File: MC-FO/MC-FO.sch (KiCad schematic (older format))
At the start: 1 part, among them J1 DB25_Female

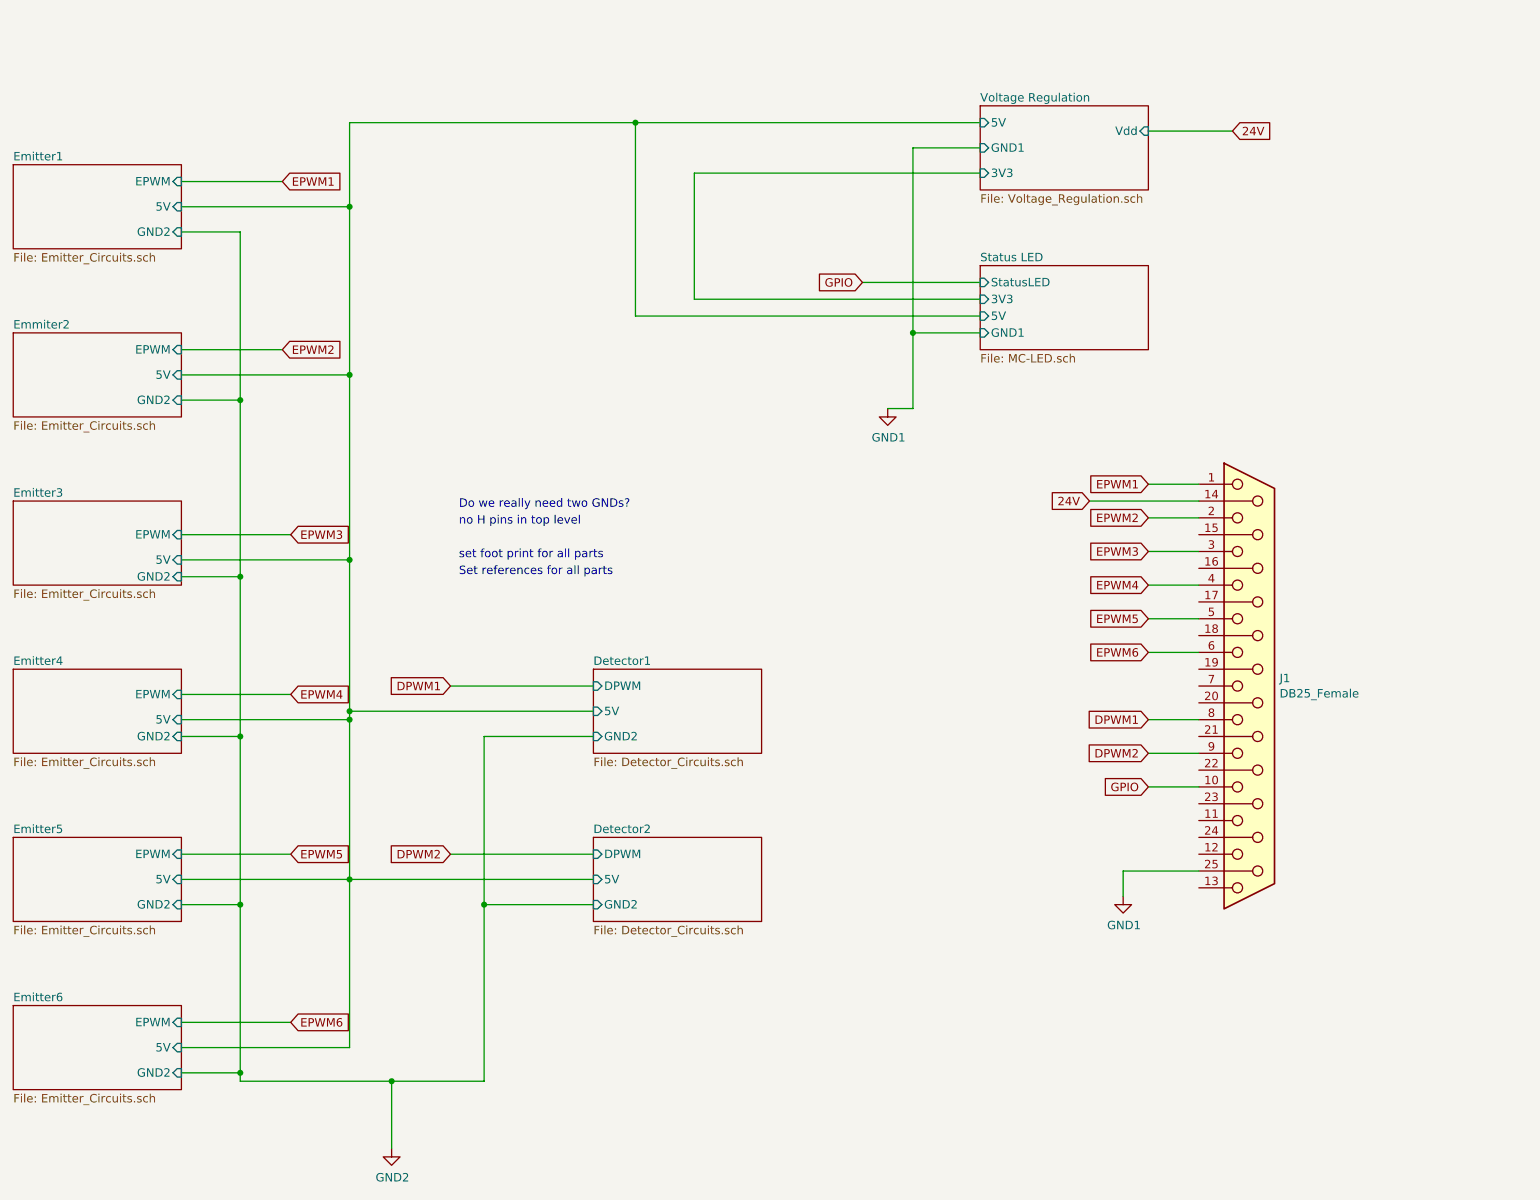
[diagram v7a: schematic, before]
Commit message: floating pins fix, signal name updates
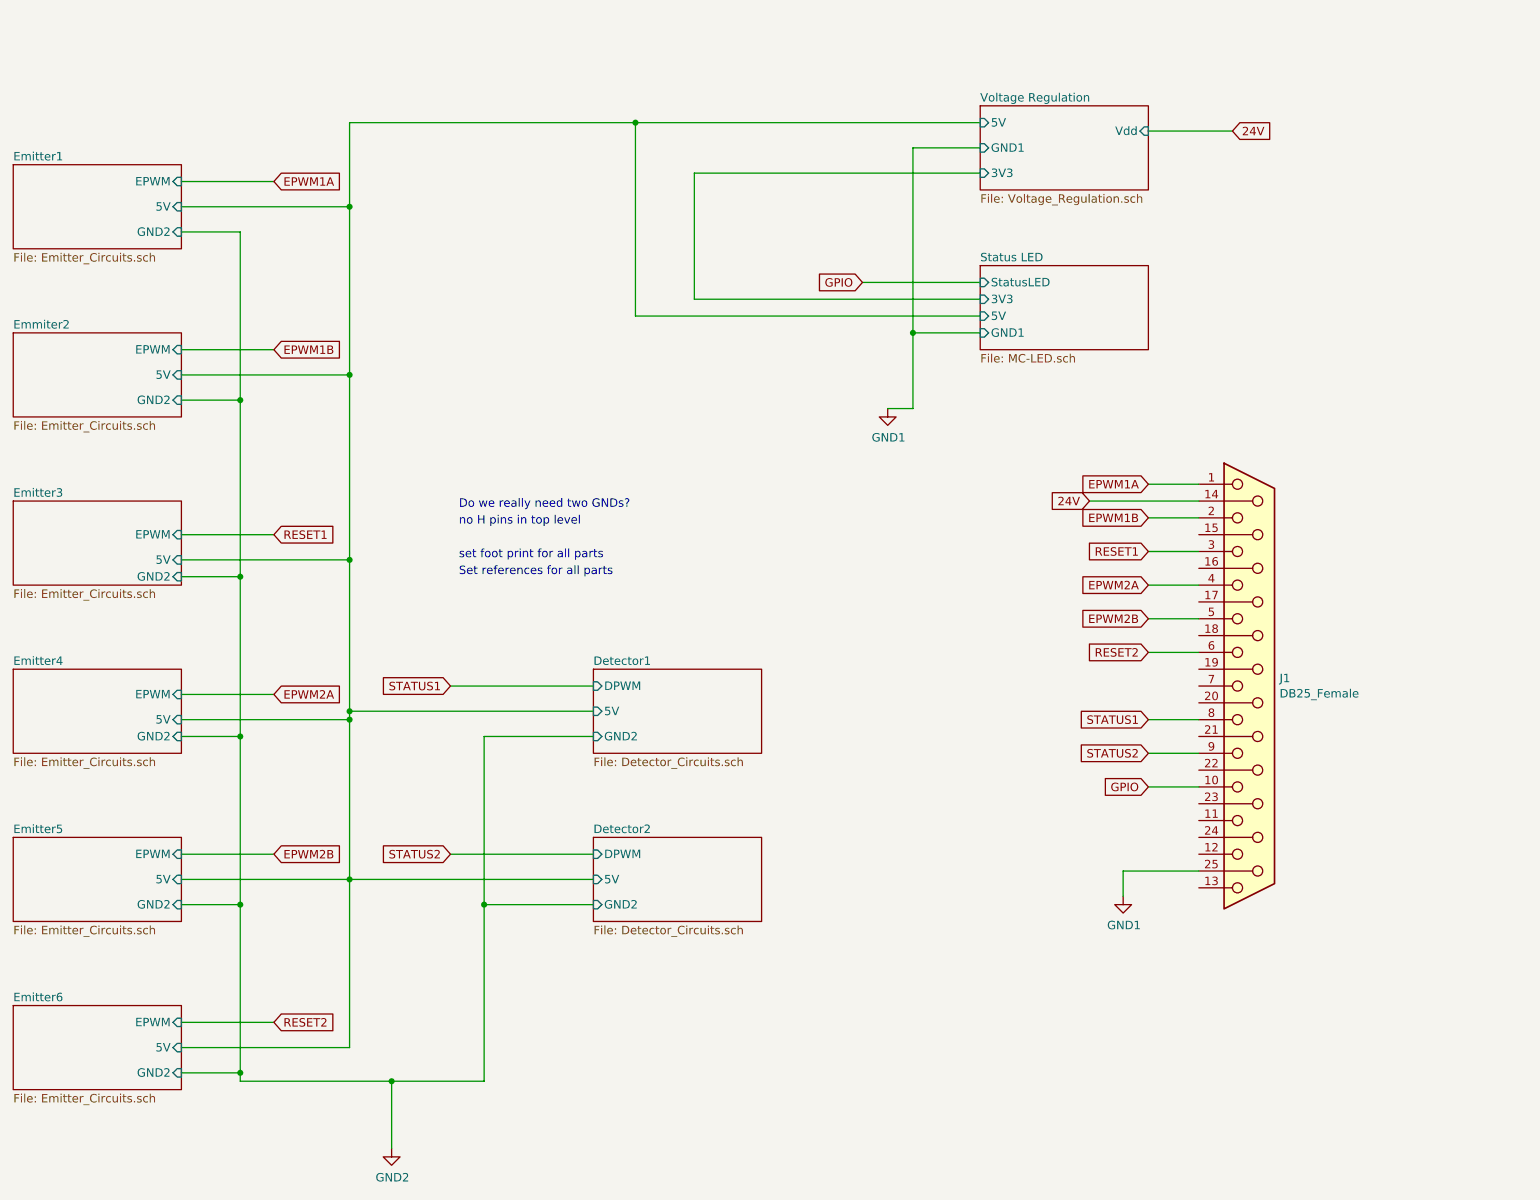
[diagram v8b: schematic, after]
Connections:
- net DPWM1 renamed STATUS1
- net DPWM2 renamed STATUS2
- net EPWM1 renamed EPWM1A
- net EPWM2 renamed EPWM1B
- net EPWM3 renamed RESET1
- net EPWM4 renamed EPWM2A
- net EPWM5 renamed EPWM2B
- net EPWM6 renamed RESET2
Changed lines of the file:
@@
 $EndSheet
-Wire Wire Line
-	2500 3700 3150 3700
-Wire Wire Line
-	2500 4650 3150 4650
-Wire Wire Line
-	2500 5600 3150 5600
-Wire Wire Line
-	2500 1600 3100 1600
 Wire Wire Line
 	3500 6750 2500 6750
@@
 	2850 2900 2850 3950
 Wire Wire Line
-	2500 6600 3150 6600
-Wire Wire Line
 	3500 4800 3500 5750
 Wire Wire Line
@@
 Text Notes 4150 3650 0    50   ~ 0
 no H pins in top level\n
-Text GLabel 3100 1600 2    50   Input ~ 0
-EPWM1
-Text GLabel 3100 2600 2    50   Input ~ 0
-EPWM2
+Text GLabel 3050 1600 2    50   Input ~ 0
+EPWM1A
+Text GLabel 3050 2600 2    50   Input ~ 0
+EPWM1B
 Text GLabel 8250 3400 0    50   Input ~ 0
-EPWM1
+EPWM1A
 Text GLabel 8250 3600 0    50   Input ~ 0
-EPWM2
+EPWM1B
 Text GLabel 8750 1300 2    50   Input ~ 0
 24V
@@
 Set references for all parts\n
 Text GLabel 8250 3800 0    50   Input ~ 0
-EPWM3
+RESET1
 Text GLabel 8250 4000 0    50   Input ~ 0
-EPWM4
+EPWM2A
 Text GLabel 8250 4200 0    50   Input ~ 0
-EPWM5
+EPWM2B
 Text GLabel 8250 4400 0    50   Input ~ 0
-EPWM6
+RESET2
 Text GLabel 8250 4800 0    50   Input ~ 0
-DPWM1
+STATUS1
 Text GLabel 8250 5000 0    50   Input ~ 0
-DPWM2
-Text GLabel 3150 3700 2    50   Input ~ 0
-EPWM3
-Text GLabel 3150 4650 2    50   Input ~ 0
-EPWM4
-Text GLabel 3150 5600 2    50   Input ~ 0
-EPWM5
-Text GLabel 3150 6600 2    50   Input ~ 0
-EPWM6
+STATUS2
+Text GLabel 3050 3700 2    50   Input ~ 0
+RESET1
+Text GLabel 3050 4650 2    50   Input ~ 0
+EPWM2A
+Text GLabel 3050 5600 2    50   Input ~ 0
+EPWM2B
+Text GLabel 3050 6600 2    50   Input ~ 0
+RESET2
 Text GLabel 8250 5200 0    50   Input ~ 0
 GPIO
@@
 	8100 5700 8100 5850
 Text GLabel 4100 4600 0    50   Input ~ 0
-DPWM1
+STATUS1
 Text GLabel 4100 5600 0    50   Input ~ 0
-DPWM2
+STATUS2
 Wire Wire Line
 	7250 1250 5200 1250
@@
 Connection ~ 3500 1750
 Connection ~ 3500 2750
-Wire Wire Line
-	3100 2600 2500 2600
 $Comp
 L power:GND1 #PWR02
@@
 Wire Wire Line
 	5200 1250 3500 1250
+Wire Wire Line
+	2500 6600 3050 6600
+Wire Wire Line
+	2500 5600 3050 5600
+Wire Wire Line
+	2500 4650 3050 4650
+Wire Wire Line
+	2500 3700 3050 3700
+Wire Wire Line
+	2500 2600 3050 2600
+Wire Wire Line
+	2500 1600 3050 1600
 $EndSCHEMATC
